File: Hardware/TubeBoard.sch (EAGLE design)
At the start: 20 parts, among them IC1 HV5530PQFP-44

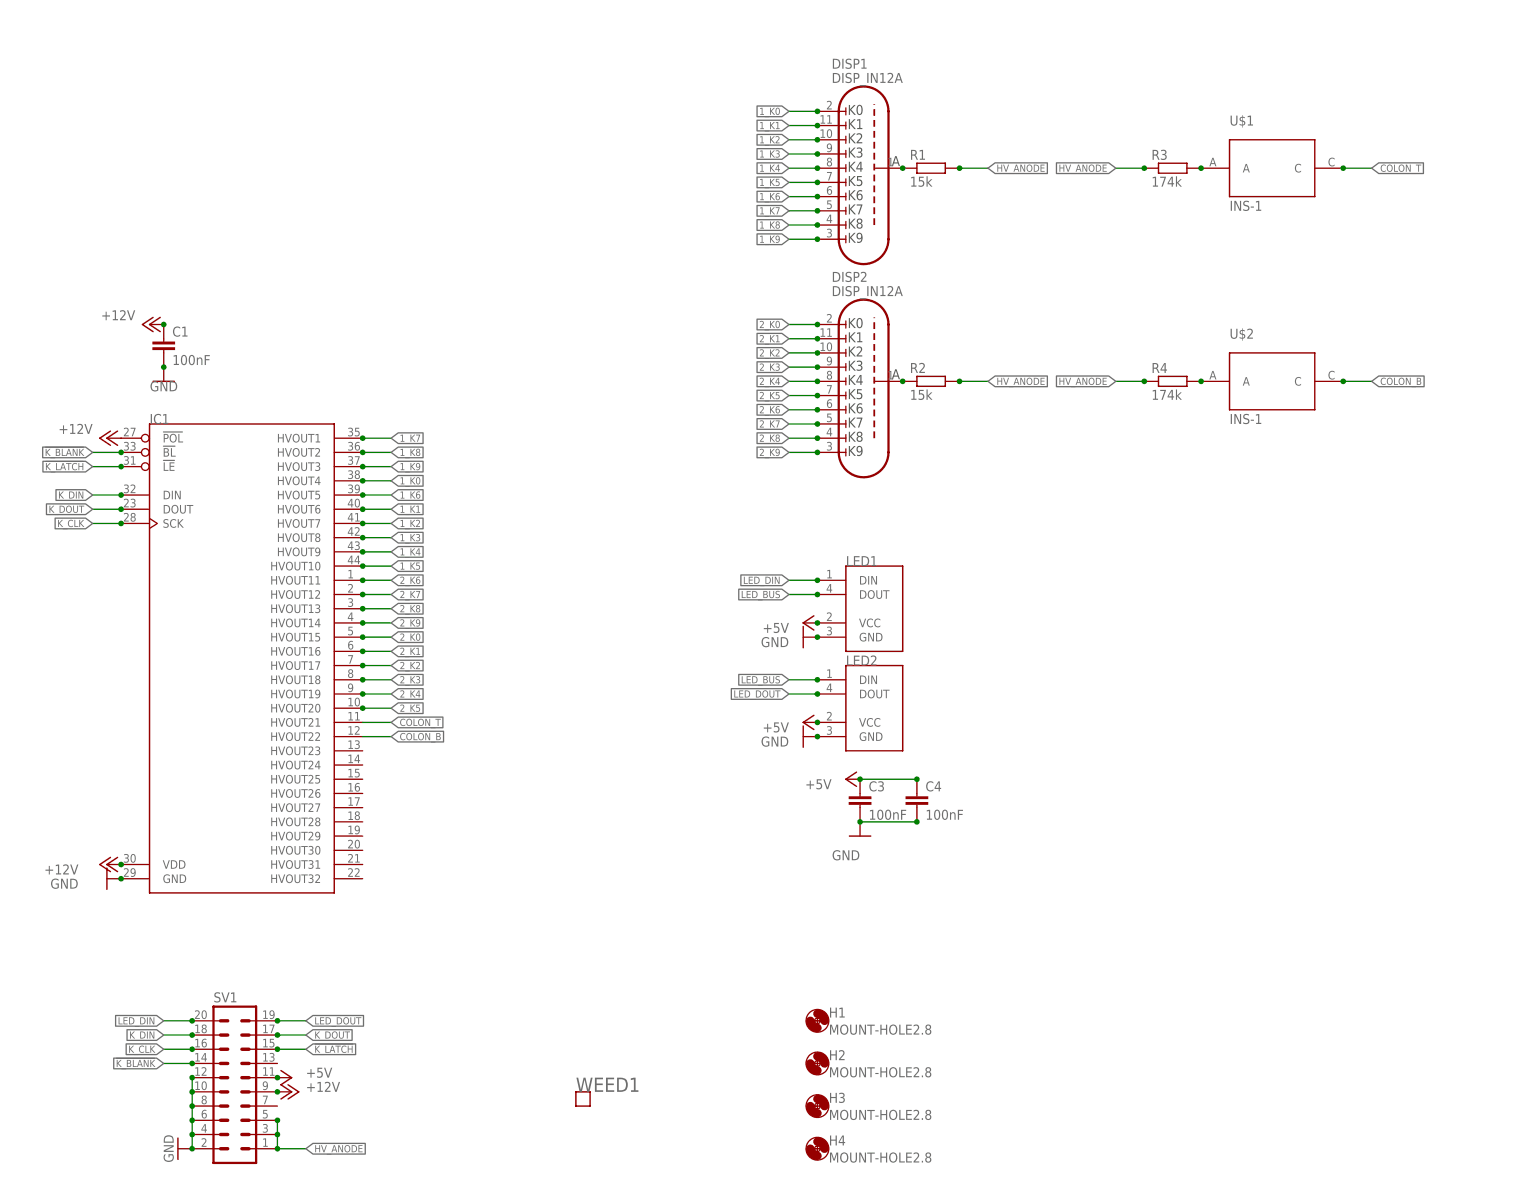
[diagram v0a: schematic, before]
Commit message: finished tube board schematic
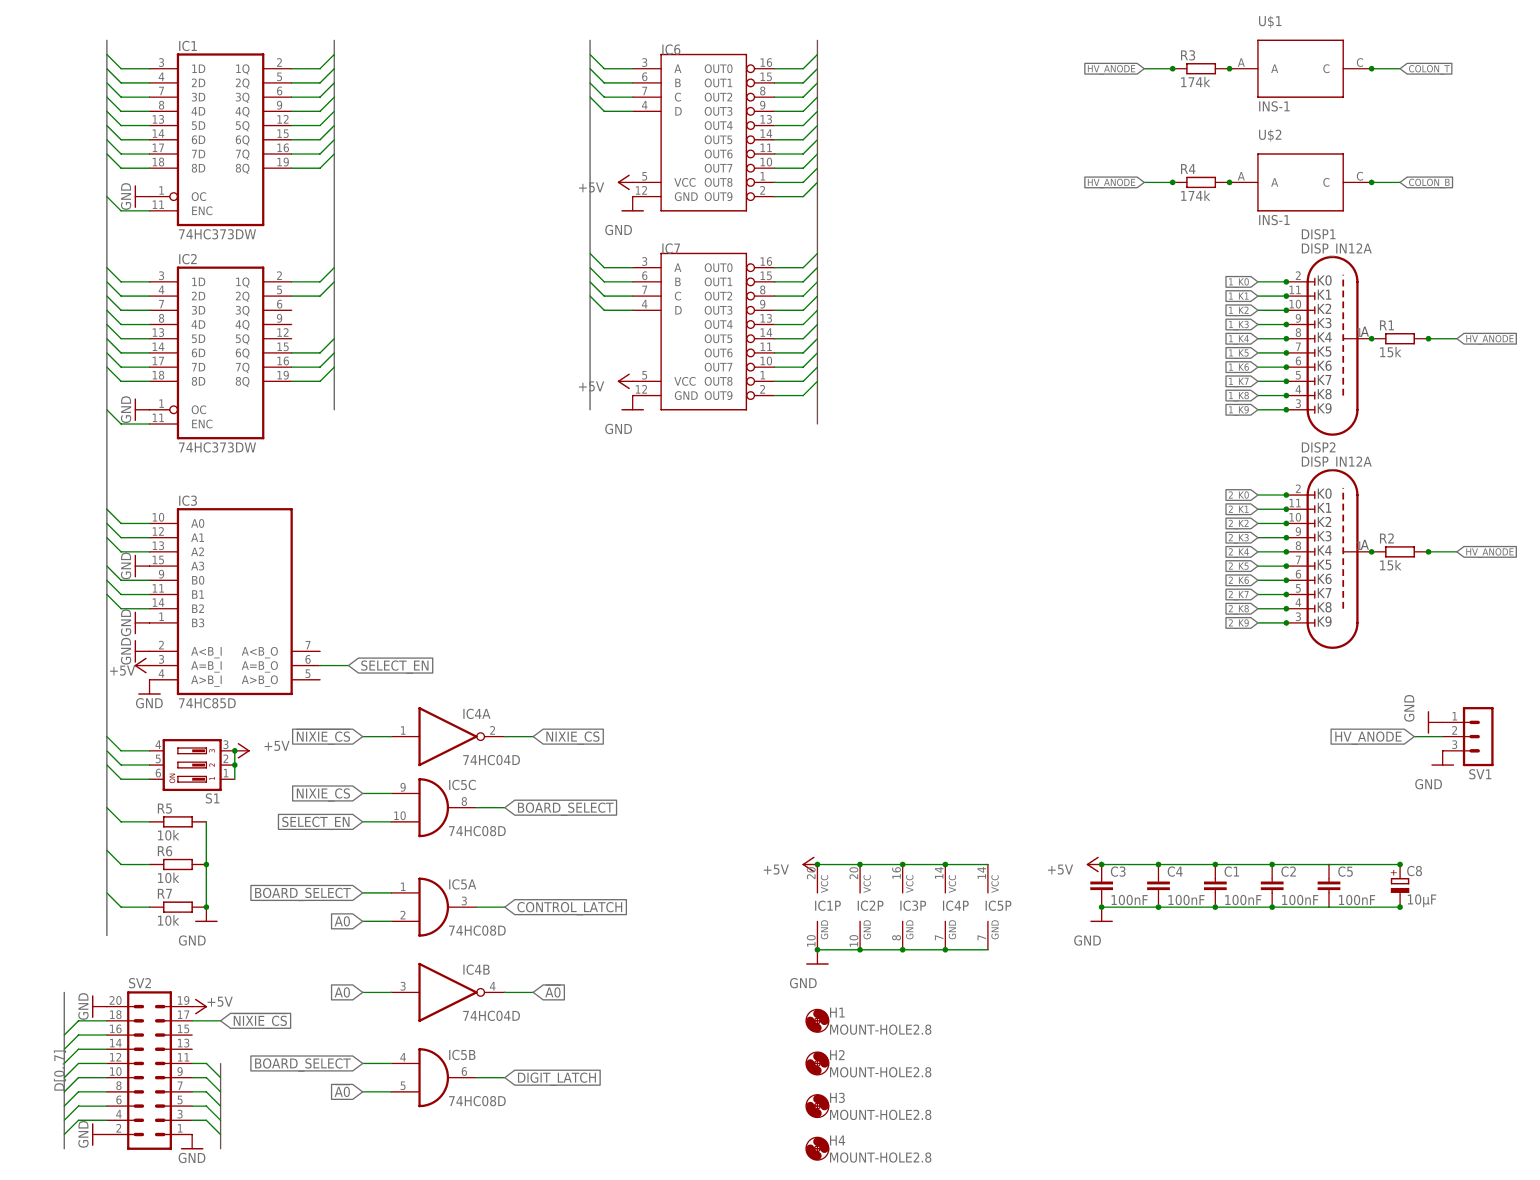
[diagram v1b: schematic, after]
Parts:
- removed LED1, LED2: (no value), Parts:NEOPIXEL-5MMLED-4PIN
- removed WEED1: WEED, Parts:WEED
- added C2, C5: 100nF, rcl:C-EUC1206
- added C8: 10µF, rcl:CPOL-EUSMCB
- added IC2: 74HC373DW, 74xx-eu:74HC373DW
- added IC3: 74HC85D, 74xx-eu:74HC85D
- added IC4: 74HC04D, 74xx-eu:74HC04D
- added IC5: 74HC08D, 74xx-eu:74HC08D
- added IC6, IC7: (no value), Parts:7441DIL16
- added R5, R6, R7: 10k, rcl:R-EU_R2012
- added S1: (no value), switch-dil:SD4-03
- added SV2: (no value), con-lstb:MA10-2
- IC1: value HV5530PQFP-44 -> 74HC373DW; device Parts:HV5530PQFP-44 -> 74xx-eu:74HC373DW
- SV1: device con-lstb:MA10-2 -> con-lstb:MA03-1
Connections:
- removed net !K_BLANK: IC1.!BL, SV1.14
- removed net !K_LATCH: IC1.!LE, SV1.15
- removed net +12V: C1.1, IC1.!POL, IC1.VDD, SV1.9
- removed net K_CLK: IC1.SCK, SV1.16
- removed net K_DIN: IC1.DIN, SV1.18
- removed net K_DOUT: IC1.DOUT, SV1.17
- removed net LED_BUS: LED1.DOUT, LED2.DIN
- removed net LED_DIN: LED1.DIN, SV1.20
- removed net LED_DOUT: LED2.DOUT, SV1.19
- new net !A0: IC4B.O, IC5B.I1
- new net !NIXIE_CS: IC4A.I, SV2.17
- new net A0: IC4B.I, IC5A.I1, SV2.3
- new net A1: SV2.5
- new net A2: IC3A.A0, SV2.7
- new net A3: IC3A.A1, SV2.9
- new net A4: IC3A.A2, SV2.11
- new net BOARD_SELECT: IC5A.I0, IC5B.I0, IC5C.O
- new net CONTROL_LATCH: IC2A.ENC, IC5A.O
- new net D0: IC1A.1D, IC2A.1D, SV2.8
- new net D1: IC1A.2D, IC2A.2D, SV2.6
- new net D2: IC1A.3D, IC2A.3D, SV2.4
- new net D3: IC1A.4D, IC2A.4D, SV2.10
- new net D4: IC1A.5D, IC2A.5D, SV2.12
- new net D5: IC1A.6D, IC2A.6D, SV2.14
- new net D6: IC1A.7D, IC2A.7D, SV2.16
- new net D7: IC1A.8D, IC2A.8D, SV2.18
- new net DIGIT_LATCH: IC1A.ENC, IC5B.O
- new net DRIVE_HI: IC2A.8Q
- new net DRIVE_LO: IC2A.6Q
- new net DRIVE_MED: IC2A.7Q
- new net ID0: IC3A.B0, R7.1, S1.6
- new net ID1: IC3A.B1, R6.1, S1.5
- new net ID2: IC3A.B2, R5.1, S1.4
- new net LDIGIT0: IC1A.1Q, IC6.A
- new net LDIGIT1: IC1A.2Q, IC6.B
- new net LDIGIT2: IC1A.3Q, IC6.C
- new net LDIGIT3: IC1A.4Q, IC6.D
- new net NIXIE_CS: IC4A.O, IC5C.I0
- new net RDIGIT0: IC1A.5Q, IC7.A
- new net RDIGIT1: IC1A.6Q, IC7.B
- new net RDIGIT2: IC1A.7Q, IC7.C
- new net RDIGIT3: IC1A.8Q, IC7.D
- new net SELECT_EN: IC3A.A=B_O, IC5C.I1
- net +5V: now also C1.1, C2.1, C5.1, C8.+, IC1P.VCC, IC2P.VCC, IC3A.A=B_I, IC3P.VCC, IC4P.VCC, IC5P.VCC, IC6.VCC, IC7.VCC, S1.1, S1.2, S1.3, SV2.19; no longer LED1.VCC, LED2.VCC, SV1.11
- net 1_K0: now also IC6.OUT0; no longer IC1.HVOUT4
- net 1_K1: now also IC6.OUT1; no longer IC1.HVOUT6
- net 1_K2: now also IC6.OUT2; no longer IC1.HVOUT7
- net 1_K3: now also IC6.OUT3; no longer IC1.HVOUT8
- net 1_K4: now also IC6.OUT4; no longer IC1.HVOUT9
- net 1_K5: now also IC6.OUT5; no longer IC1.HVOUT10
- net 1_K6: now also IC6.OUT6; no longer IC1.HVOUT5
- net 1_K7: now also IC6.OUT7; no longer IC1.HVOUT1
- net 1_K8: now also IC6.OUT8; no longer IC1.HVOUT2
- net 1_K9: now also IC6.OUT9; no longer IC1.HVOUT3
- net 2_K0: now also IC7.OUT0; no longer IC1.HVOUT15
- net 2_K1: now also IC7.OUT1; no longer IC1.HVOUT16
- net 2_K2: now also IC7.OUT2; no longer IC1.HVOUT17
- net 2_K3: now also IC7.OUT3; no longer IC1.HVOUT18
- net 2_K4: now also IC7.OUT4; no longer IC1.HVOUT19
- net 2_K5: now also IC7.OUT5; no longer IC1.HVOUT20
- net 2_K6: now also IC7.OUT6; no longer IC1.HVOUT11
- net 2_K7: now also IC7.OUT7; no longer IC1.HVOUT12
- net 2_K8: now also IC7.OUT8; no longer IC1.HVOUT13
- net 2_K9: now also IC7.OUT9; no longer IC1.HVOUT14
- net COLON_B: now also IC2A.1Q; no longer IC1.HVOUT22
- net COLON_T: now also IC2A.2Q; no longer IC1.HVOUT21
- net GND: now also C2.2, C5.2, C8.-, IC1A.OC, IC1P.GND, IC2A.OC, IC2P.GND, IC3A.A3, IC3A.A<B_I, IC3A.A>B_I, IC3A.B3, IC3P.GND, IC4P.GND, IC5P.GND, IC6.GND, IC7.GND, R5.2, R6.2, R7.2, SV1.1, SV1.3, SV2.1, SV2.2, SV2.20; no longer IC1.GND, LED1.GND, LED2.GND, SV1.10, SV1.12, SV1.2, SV1.4, SV1.6, SV1.8
- net HV_ANODE: now also SV1.2; no longer SV1.1, SV1.3, SV1.5
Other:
- moved on the sheet: C1, C3, C4, DISP1, DISP2, R1, R2, R3, R4, U$1, U$2

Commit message: added transistors to drive colons
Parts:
- added R8, R9: 10k, rcl:R-EU_R2012
- added T1, T2: MPSA42, transistor:MPSA42-NPN-TO92-EBC
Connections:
- new net K_COLON_B: T1.C, U$2.C
- new net K_COLON_T: T2.C, U$1.C
- new net N$5: R8.2, T1.B
- new net N$6: R9.2, T2.B
- net COLON_B: now also R8.1; no longer U$2.C
- net COLON_T: now also R9.1; no longer U$1.C
- net GND: now also T1.E, T2.E
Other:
- moved on the sheet: IC6, IC7
